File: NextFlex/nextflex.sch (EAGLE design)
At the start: 2 parts, among them J1 FFC-32, J2 FFC-32

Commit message: more nextflex progress
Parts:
- added C1, C2, C7, C8: 1uF, scono:CAP0603-CAP
- added C3, C4: 18pF, scono:CAP0603-CAP
- added C5, C6: 2.2uF, scono:CAP0603-CAP
- added D1, D2: (no value), scono:DIODE_CZRU
- added D4, D7: RED, scono:LED0603
- added D5: NIR, scono:LED0603
- added D6: OPD, scono:LED1206
- added D8: YELLOW, scono:LED0603
- added D9: GREEN, scono:LED0603
- added J3: (no value), scono:CONN_10"
- added J4, J5: (no value), scono:CONN_02
- added J6: (no value), scono:CONN_06SILK_FEMALE_PTH
- added J7: (no value), scono:CONN_04
- added J8: FFC-32, scono:FFC-32
- added JP1, JP2: JUMPER-SMT_2_NC_TRACE_NO-SILK, scono:JUMPER-SMT_2_NC_TRACE_NO-SILK
- added Q1: (no value), scono:CRYSTAL_ECS_8MHZ
- added R1, R2: 10k, scono:R-US_0603
- added R3: 330R, scono:RES_BUS
- added R7, R8: 330R, scono:R-US_0603
- added R9: 1k, scono:R-US_0603
- added R_CAL, R_FB: 100k, scono:R-US_0603
- added S1: (no value), scono:DP3T
- added TP3, TP4, VIN, VOUT: TEST_POINTTHRU, scono:TEST_POINTTHRU
- added U1, U2: DG406DYZ-T, scono:DG406DYZ-T
- added U3: AD5933YRSZ, scono:AD5933YRSZ
- added U4: AFE4490_AFE4490, scono:AFE4490_AFE4490
- added U5: AZ1117EH-3.3TRG1, scono:AZ1117EH-3.3TRG1
- added U6: LM340SX-5.0/NOPB, scono:LM340SX-5.0/NOPB
- J2: value FFC-32 -> (none); device scono:FFC-32 -> scono:CONN_02
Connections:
- new net 3.3V: C2.1, C7.1, D7.A, JP2.2, U4.!AFE_PDN, U4.!RESET, U4.RX_ANA_SUP@1, U4.RX_ANA_SUP@2, U4.RX_DIG_SUP, U5.OUT
- new net 5V: C8.1, J6.6, U4.LED_DRV_SUP@1, U4.LED_DRV_SUP@2, U4.TX_CTRL_SUP, U5.IN
- new net 9V: J8.11, J8.12, J8.27, J8.28
- new net ADC_RDY: U4.ADC_RDY
- new net BG: C5.1, U4.BG
- new net E1: J1.1, J1.2, U1.S1, U2.S1
- new net E10: J1.19, J1.20, U1.S10, U2.S10
- new net E11: J1.21, J1.22, U1.S11, U2.S11
- new net E12: J1.23, J1.24, U1.S12, U2.S12
- new net E13: J1.25, J1.26, U1.S13, U2.S13
- new net E14: J1.27, J1.28, U1.S14, U2.S14
- new net E15: J1.29, J1.30, U1.S15, U2.S15
- new net E2: J1.3, J1.4, U1.S2, U2.S2
- new net E3: J1.5, J1.6, U1.S3, U2.S3
- new net E4: J1.7, J1.8, U1.S4, U2.S4
- new net E5: J1.10, J1.9, U1.S5, U2.S5
- new net E6: J1.11, J1.12, U1.S6, U2.S6
- new net E7: J1.13, J1.14, U1.S7, U2.S7
- new net E8: J1.15, J1.16, U1.S8, U2.S8
- new net E9: J1.17, J1.18, U1.S9, U2.S9
- new net GND: C1.1, C2.2, C3.2, C4.2, C5.2, C6.2, C7.2, C8.2, D1.P, D2.P, J5.1, J5.2, J6.1, R3.10, R3.11, R3.12, R3.13, R3.14, R3.15, R3.16, R3.9, U1.GND, U1.V-, U2.GND, U2.V-, U3.AGND1, U3.AGND2, U3.DGND, U4.LED_DRV_GND@1, U4.LED_DRV_GND@2, U4.LED_DRV_GND@3, U4.RX_ANA_GND@1, U4.RX_ANA_GND@2, U4.RX_ANA_GND@3, U4.RX_DIG_GND@1, U4.RX_DIG_GND@2, U4.VSS, U5.ADJ/GND
- new net GRN: D9.A
- new net INN: J7.4, J8.19, J8.20, JP1.2, U4.INN
- new net INP: D6.C, J7.3, J8.23, J8.24, U4.INP
- new net MUX_1_16: R_CAL.1, TP4.P$1, U1.S16
- new net MUX_1_SEL_0: J3.3, U1.A0
- new net MUX_1_SEL_1: J3.4, U1.A1
- new net MUX_1_SEL_2: J3.5, U1.A2
- new net MUX_1_SEL_3: J3.6, U1.A3
- new net MUX_2_16: R_CAL.2, TP3.P$1, U2.S16
- new net MUX_2_SEL_0: J3.7, U2.A0
- new net MUX_2_SEL_1: J3.8, U2.A1
- new net MUX_2_SEL_2: J3.9, U2.A2
- new net MUX_2_SEL_3: J3.10, U2.A3
- new net N$16: D4.A, D5.A, JP2.1
- new net N$17: D5.C, R7.1
- new net N$18: D4.C, R8.1
- new net N$19: D6.A, R9.1
- new net N$20: JP1.1, R9.2
- new net N$3: R_FB.2, U3.RFB
- new net N$5: D7.C, R3.1, R3.2
- new net N$6: D8.C, R3.4, R3.5
- new net N$7: D9.C, R3.7, R3.8
- new net SCL: J3.2, R2.1, U3.SCL
- new net SDA: J3.1, R1.1, U3.SDA
- new net SPI_MISO: J6.3, U4.SPISOMI
- new net SPI_MOSI: J6.4, U4.SPISIMO
- new net SPI_SCLK: J6.2, U4.SCLK
- new net SPI_SEL: J6.5, U4.SPISTE
- new net TXN: D1.N, J7.1, J8.15, J8.16, R7.2, U4.TXN
- new net TXP: D2.N, J7.2, J8.31, J8.32, R8.2, U4.TXP
- new net TX_REF: C6.1, U4.TX_REF
- new net VCC: C1.2, J4.1, J4.2, R1.2, R2.2, U1.EN, U1.V+, U2.EN, U2.V+, U3.AVDD1, U3.AVDD2, U3.DVDD
- new net VIN: J2.1, U2.D, VIN.P$1
- new net VIN_AD: J2.2, R_FB.1, U3.VIN
- new net VOUT: U1.D, U3.VOUT, VOUT.P$1
- new net XIN: C3.1, Q1.A, U4.XIN
- new net XOUT: C4.1, Q1.B, U4.XOUT
- new net YEL: D8.A
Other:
- note added: "AFE4490 SPI"

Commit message: finish rev a of nextflex
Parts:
- removed D7: RED, scono:LED0603
- removed D8: YELLOW, scono:LED0603
- removed D9: GREEN, scono:LED0603
- removed J8: FFC-32, scono:FFC-32
- removed R3: 330R, scono:RES_BUS
- removed S1: (no value), scono:DP3T
- added S2: DPDT-SWITCH, scono:DPDT-SWITCH
- J4: value (none) -> BAT
- J5: value (none) -> FFC-32; device scono:CONN_02 -> scono:FFC-32
- J6: device scono:CONN_06SILK_FEMALE_PTH -> scono:CONN_04
- Q1: device scono:CRYSTAL_ECS_8MHZ -> scono:CRYSTAL_SMOL
- U6: value LM340SX-5.0/NOPB -> LM340MPX-5.0230; device scono:LM340SX-5.0/NOPB -> scono:LM340MPX-5.0230
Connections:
- removed net 9V: J8.11, J8.12, J8.27, J8.28
- removed net GRN: D9.A
- removed net N$5: D7.C, R3.1, R3.2
- removed net N$6: D8.C, R3.4, R3.5
- removed net N$7: D9.C, R3.7, R3.8
- removed net YEL: D8.A
- new net BAT+: J4.2, S2.1
- new net BAT-: J4.1, S2.4
- net 3.3V: no longer D7.A
- net 5V: now also C1.2, R1.2, R2.2, U1.EN, U1.V+, U2.EN, U2.V+, U3.AVDD1, U3.AVDD2, U3.DVDD, U6.5V; no longer J6.6
- net E1: now also J1.31, J1.32; no longer J1.1, J1.2
- net E10: now also J1.13, J1.14; no longer J1.19, J1.20
- net E11: now also J1.11, J1.12; no longer J1.21, J1.22
- net E12: now also J1.10, J1.9; no longer J1.23, J1.24
- net E13: now also J1.7, J1.8; no longer J1.25, J1.26
- net E14: now also J1.5, J1.6; no longer J1.27, J1.28
- net E15: now also J1.3, J1.4; no longer J1.29, J1.30
- net E2: now also J1.29, J1.30; no longer J1.3, J1.4
- net E3: now also J1.27, J1.28; no longer J1.5, J1.6
- net E4: now also J1.25, J1.26; no longer J1.7, J1.8
- net E5: now also J1.23, J1.24; no longer J1.10, J1.9
- net E6: now also J1.21, J1.22; no longer J1.11, J1.12
- net E7: now also J1.19, J1.20; no longer J1.13, J1.14
- net E8: now also J1.17, J1.18; no longer J1.15, J1.16
- net E9: now also J1.15, J1.16; no longer J1.17, J1.18
- net GND: now also S2.5, U6.GND; no longer J5.1, J5.2, J6.1, R3.10, R3.11, R3.12, R3.13, R3.14, R3.15, R3.16, R3.9
- net INN: now also J5.10, J5.9, J7.3; no longer J7.4, J8.19, J8.20
- net INP: now also J5.13, J5.14, J7.2; no longer J7.3, J8.23, J8.24
- net SPI_MOSI: now also J6.2; no longer J6.4
- net SPI_SCLK: now also J6.4; no longer J6.2
- net SPI_SEL: now also J6.1; no longer J6.5
- net TXN: now also J5.5, J5.6, J7.4; no longer J7.1, J8.15, J8.16
- net TXP: now also J5.21, J5.22, J7.1; no longer J7.2, J8.31, J8.32
- net VCC: now also J5.1, J5.17, J5.18, J5.2, S2.2, U6.VIN; no longer C1.2, J4.1, J4.2, R1.2, R2.2, U1.EN, U1.V+, U2.EN, U2.V+, U3.AVDD1, U3.AVDD2, U3.DVDD

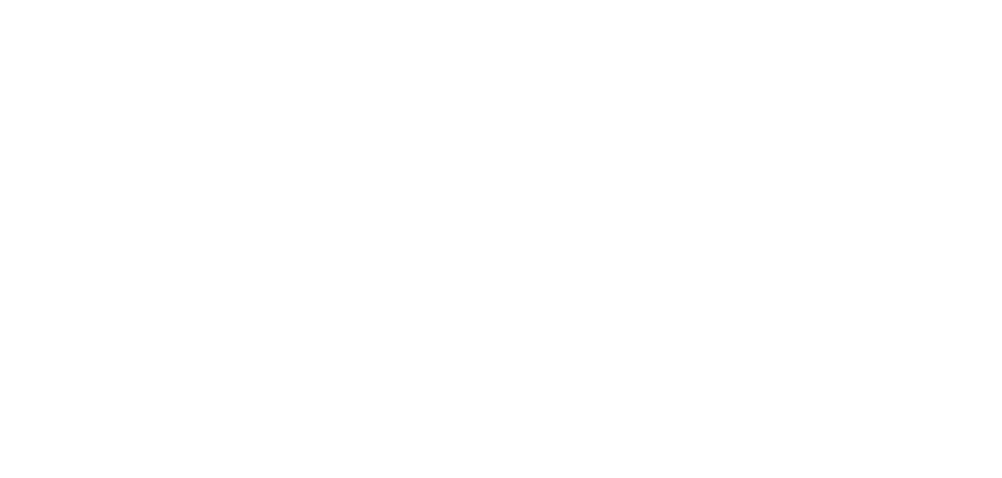
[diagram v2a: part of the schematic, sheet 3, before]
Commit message: Add bom and clp files for jcl
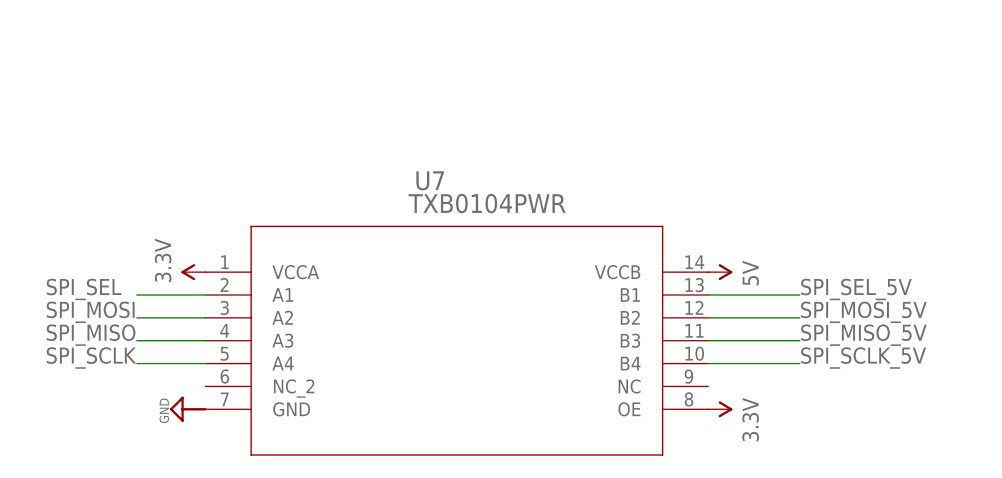
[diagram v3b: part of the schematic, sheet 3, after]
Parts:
- added U7: TXB0104PWR, scono:TXB0104PWR
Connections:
- new net SPI_MISO_5V: J6.3, U7.B3
- new net SPI_MOSI_5V: J6.2, U7.B2
- new net SPI_SCLK_5V: J6.4, U7.B4
- new net SPI_SEL_5V: J6.1, U7.B1
- net 3.3V: now also U7.OE, U7.VCCA
- net 5V: now also U7.VCCB
- net GND: now also U7.GND
- net SPI_MISO: now also U7.A3; no longer J6.3
- net SPI_MOSI: now also U7.A2; no longer J6.2
- net SPI_SCLK: now also U7.A4; no longer J6.4
- net SPI_SEL: now also U7.A1; no longer J6.1
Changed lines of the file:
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@@
 <part name="J5" library="scono" library_urn="urn:adsk.eagle:library:14850048" deviceset="FFC-32" device="" package3d_urn="urn:adsk.eagle:package:14850860/1"/>
 <part name="J6" library="scono" library_urn="urn:adsk.eagle:library:14850048" deviceset="CONN_04" device="" package3d_urn="urn:adsk.eagle:package:38085/1"/>
+<part name="U7" library="scono" library_urn="urn:adsk.eagle:library:14850048" deviceset="TXB0104PWR" device="" package3d_urn="urn:adsk.eagle:package:14850851/1"/>
+<part name="U$2" library="scono" library_urn="urn:adsk.eagle:library:14850048" deviceset="5V" device=""/>
+<part name="U$13" library="scono" library_urn="urn:adsk.eagle:library:14850048" deviceset="3.3V" device=""/>
+<part name="SUPPLY6" library="scono" library_urn="urn:adsk.eagle:library:14850048" deviceset="GND" device=""/>
+<part name="U$14" library="scono" library_urn="urn:adsk.eagle:library:14850048" deviceset="3.3V" device=""/>
 </parts>
 <sheets>
@@
 <pinref part="U4" gate="G$1" pin="SCLK"/>
 </segment>
-<segment>
-<pinref part="J6" gate="G$1" pin="4"/>
-<wire x1="175.26" y1="83.82" x2="177.8" y2="83.82" width="0.1524" layer="91"/>
-<label x="177.8" y="83.82" size="1.778" layer="95"/>
-</segment>
 </net>
 <net name="SPI_MOSI" class="0">
@@
 <pinref part="U4" gate="G$1" pin="SPISIMO"/>
 </segment>
-<segment>
-<pinref part="J6" gate="G$1" pin="2"/>
-<wire x1="175.26" y1="78.74" x2="177.8" y2="78.74" width="0.1524" layer="91"/>
-<label x="177.8" y="78.74" size="1.778" layer="95"/>
-</segment>
 </net>
 <net name="SPI_SEL" class="0">
@@
 <pinref part="U4" gate="G$1" pin="SPISTE"/>
 </segment>
-<segment>
-<pinref part="J6" gate="G$1" pin="1"/>
-<wire x1="175.26" y1="76.2" x2="177.8" y2="76.2" width="0.1524" layer="91"/>
-<label x="177.8" y="76.2" size="1.778" layer="95"/>
-</segment>
 </net>
 <net name="SPI_MISO" class="0">
@@
 <label x="93.98" y="137.16" size="1.778" layer="95"/>
 <pinref part="U4" gate="G$1" pin="SPISOMI"/>
-</segment>
-<segment>
-<pinref part="J6" gate="G$1" pin="3"/>
-<wire x1="175.26" y1="81.28" x2="177.8" y2="81.28" width="0.1524" layer="91"/>
-<label x="177.8" y="81.28" size="1.778" layer="95"/>
 </segment>
 </net>
@@
 <pinref part="J5" gate="G$1" pin="18"/>
 <wire x1="116.84" y1="55.88" x2="116.84" y2="53.34" width="0.1524" layer="91"/>
+</segment>
+</net>
+<net name="SPI_SCLK_5V" class="0">
+<segment>
+<pinref part="J6" gate="G$1" pin="4"/>
+<wire x1="175.26" y1="83.82" x2="177.8" y2="83.82" width="0.1524" layer="91"/>
+<label x="177.8" y="83.82" size="1.778" layer="95"/>
+</segment>
+</net>
+<net name="SPI_MISO_5V" class="0">
+<segment>
+<pinref part="J6" gate="G$1" pin="3"/>
+<wire x1="175.26" y1="81.28" x2="177.8" y2="81.28" width="0.1524" layer="91"/>
+<label x="177.8" y="81.28" size="1.778" layer="95"/>
+</segment>
+</net>
+<net name="SPI_MOSI_5V" class="0">
+<segment>
+<pinref part="J6" gate="G$1" pin="2"/>
+<wire x1="175.26" y1="78.74" x2="177.8" y2="78.74" width="0.1524" layer="91"/>
+<label x="177.8" y="78.74" size="1.778" layer="95"/>
+</segment>
+</net>
+<net name="SPI_SEL_5V" class="0">
+<segment>
+<pinref part="J6" gate="G$1" pin="1"/>
+<wire x1="175.26" y1="76.2" x2="177.8" y2="76.2" width="0.1524" layer="91"/>
+<label x="177.8" y="76.2" size="1.778" layer="95"/>
 </segment>
 </net>
@@
 <attribute name="NAME" x="48.26" y="114.808" size="1.778" layer="95" font="vector"/>
 </instance>
+<instance part="U7" gate="A" x="50.8" y="63.5" smashed="yes">
+<attribute name="NAME" x="76.5556" y="72.6186" size="2.0828" layer="95" ratio="6" rot="SR0"/>
+<attribute name="VALUE" x="75.9206" y="70.0786" size="2.0828" layer="96" ratio="6" rot="SR0"/>
+</instance>
+<instance part="U$2" gate="G$1" x="109.22" y="63.5" smashed="yes" rot="R270">
+<attribute name="VALUE" x="113.03" y="64.77" size="1.778" layer="96" rot="R270"/>
+</instance>
+<instance part="U$13" gate="G$1" x="53.34" y="63.5" smashed="yes" rot="R90">
+<attribute name="VALUE" x="49.53" y="62.23" size="1.778" layer="96" rot="R90"/>
+</instance>
+<instance part="SUPPLY6" gate="GND" x="50.8" y="48.26" smashed="yes" rot="R270">
+<attribute name="VALUE" x="48.26" y="49.53" size="1.016" layer="96" rot="R270"/>
+</instance>
+<instance part="U$14" gate="G$1" x="109.22" y="48.26" smashed="yes" rot="R270">
+<attribute name="VALUE" x="113.03" y="49.53" size="1.778" layer="96" rot="R270"/>
+</instance>
 </instances>
 <busses>
@@
 <pinref part="U$12" gate="G$1" pin="5V"/>
 </segment>
+<segment>
+<pinref part="U7" gate="A" pin="VCCB"/>
+<pinref part="U$2" gate="G$1" pin="5V"/>
+</segment>
 </net>
 <net name="GND" class="0">
@@
 <pinref part="S2" gate="G$1" pin="5"/>
 <pinref part="SUPPLY4" gate="GND" pin="GND"/>
+</segment>
+<segment>
+<pinref part="U7" gate="A" pin="GND"/>
+<pinref part="SUPPLY6" gate="GND" pin="GND"/>
 </segment>
 </net>
@@
 </segment>
 </net>
+<net name="3.3V" class="1">
+<segment>
+<pinref part="U7" gate="A" pin="VCCA"/>
+<pinref part="U$13" gate="G$1" pin="3.3V"/>
+</segment>
+<segment>
+<pinref part="U7" gate="A" pin="OE"/>
+<pinref part="U$14" gate="G$1" pin="3.3V"/>
+</segment>
+</net>
+<net name="SPI_SEL" class="0">
+<segment>
+<pinref part="U7" gate="A" pin="A1"/>
+<wire x1="53.34" y1="60.96" x2="45.72" y2="60.96" width="0.1524" layer="91"/>
+<label x="35.56" y="60.96" size="1.778" layer="95"/>
+</segment>
+</net>
+<net name="SPI_MOSI" class="0">
+<segment>
+<pinref part="U7" gate="A" pin="A2"/>
+<wire x1="53.34" y1="58.42" x2="45.72" y2="58.42" width="0.1524" layer="91"/>
+<label x="35.56" y="58.42" size="1.778" layer="95"/>
+</segment>
+</net>
+<net name="SPI_MISO" class="0">
+<segment>
+<pinref part="U7" gate="A" pin="A3"/>
+<wire x1="53.34" y1="55.88" x2="45.72" y2="55.88" width="0.1524" layer="91"/>
+<label x="35.56" y="55.88" size="1.778" layer="95"/>
+</segment>
+</net>
+<net name="SPI_SCLK" class="0">
+<segment>
+<pinref part="U7" gate="A" pin="A4"/>
+<wire x1="53.34" y1="53.34" x2="45.72" y2="53.34" width="0.1524" layer="91"/>
+<label x="35.56" y="53.34" size="1.778" layer="95"/>
+</segment>
+</net>
+<net name="SPI_SEL_5V" class="0">
+<segment>
+<pinref part="U7" gate="A" pin="B1"/>
+<wire x1="109.22" y1="60.96" x2="119.38" y2="60.96" width="0.1524" layer="91"/>
+<label x="119.38" y="60.96" size="1.778" layer="95"/>
+</segment>
+</net>
+<net name="SPI_MOSI_5V" class="0">
+<segment>
+<pinref part="U7" gate="A" pin="B2"/>
+<wire x1="109.22" y1="58.42" x2="119.38" y2="58.42" width="0.1524" layer="91"/>
+<label x="119.38" y="58.42" size="1.778" layer="95"/>
+</segment>
+</net>
+<net name="SPI_MISO_5V" class="0">
+<segment>
+<pinref part="U7" gate="A" pin="B3"/>
+<wire x1="109.22" y1="55.88" x2="119.38" y2="55.88" width="0.1524" layer="91"/>
+<label x="119.38" y="55.88" size="1.778" layer="95"/>
+</segment>
+</net>
+<net name="SPI_SCLK_5V" class="0">
+<segment>
+<pinref part="U7" gate="A" pin="B4"/>
+<wire x1="109.22" y1="53.34" x2="119.38" y2="53.34" width="0.1524" layer="91"/>
+<label x="119.38" y="53.34" size="1.778" layer="95"/>
+</segment>
+</net>

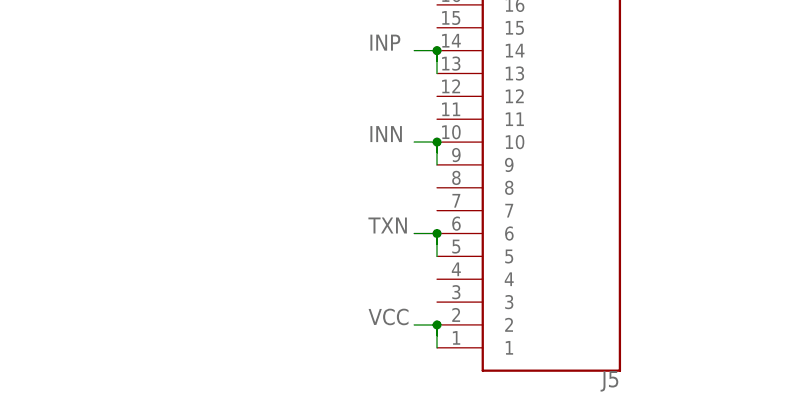
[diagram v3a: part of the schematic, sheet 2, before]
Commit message: small fixes for anode cathone config
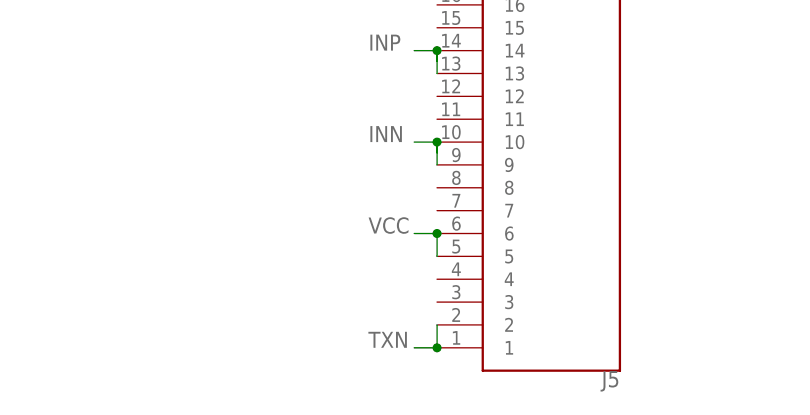
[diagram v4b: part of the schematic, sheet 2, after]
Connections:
- net TXN: now also J5.1, J5.2; no longer J5.5, J5.6
- net VCC: now also J5.5, J5.6; no longer J5.1, J5.2
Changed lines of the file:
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@@
 <?xml version="1.0" encoding="utf-8"?>
 <!DOCTYPE eagle SYSTEM "eagle.dtd">
-<eagle version="9.5.1">
+<eagle version="9.5.2">
 <drawing>
 <settings>
@@
 </segment>
 <segment>
-<wire x1="116.84" y1="25.4" x2="114.3" y2="25.4" width="0.1524" layer="91"/>
-<label x="109.22" y="25.4" size="1.778" layer="95"/>
-<wire x1="116.84" y1="25.4" x2="116.84" y2="24.2062" width="0.1524" layer="91"/>
-<junction x="116.84" y="25.4"/>
-<pinref part="J5" gate="G$1" pin="5"/>
-<pinref part="J5" gate="G$1" pin="6"/>
-<wire x1="116.84" y1="25.4" x2="116.84" y2="22.86" width="0.1524" layer="91"/>
-</segment>
-<segment>
 <pinref part="R7" gate="G$1" pin="2"/>
 <wire x1="50.8" y1="55.88" x2="53.34" y2="55.88" width="0.1524" layer="91"/>
@@
 <wire x1="93.98" y1="63.5" x2="96.52" y2="63.5" width="0.1524" layer="91"/>
 <label x="96.52" y="63.5" size="1.778" layer="95"/>
+</segment>
+<segment>
+<pinref part="J5" gate="G$1" pin="2"/>
+<pinref part="J5" gate="G$1" pin="1"/>
+<wire x1="116.84" y1="15.24" x2="116.84" y2="12.7" width="0.1524" layer="91"/>
+<wire x1="114.3" y1="12.7" x2="116.84" y2="12.7" width="0.1524" layer="91"/>
+<junction x="116.84" y="12.7"/>
+<label x="109.22" y="12.7" size="1.778" layer="95"/>
 </segment>
 </net>
@@
 <net name="VCC" class="1">
 <segment>
-<wire x1="116.84" y1="15.24" x2="114.3" y2="15.24" width="0.1524" layer="91"/>
-<label x="109.22" y="15.24" size="1.778" layer="95"/>
-<wire x1="116.84" y1="15.24" x2="116.84" y2="14.0462" width="0.1524" layer="91"/>
-<junction x="116.84" y="15.24"/>
-<pinref part="J5" gate="G$1" pin="1"/>
-<pinref part="J5" gate="G$1" pin="2"/>
-<wire x1="116.84" y1="12.7" x2="116.84" y2="15.24" width="0.1524" layer="91"/>
-</segment>
-<segment>
 <wire x1="116.84" y1="55.88" x2="114.3" y2="55.88" width="0.1524" layer="91"/>
 <label x="109.22" y="55.88" size="1.778" layer="95"/>
@@
 <wire x1="116.84" y1="55.88" x2="116.84" y2="53.34" width="0.1524" layer="91"/>
 </segment>
-</net>
+<segment>
+<pinref part="J5" gate="G$1" pin="5"/>
+<pinref part="J5" gate="G$1" pin="6"/>
+<wire x1="116.84" y1="22.86" x2="116.84" y2="25.4" width="0.1524" layer="91"/>
+<wire x1="114.3" y1="25.4" x2="116.84" y2="25.4" width="0.1524" layer="91"/>
+<junction x="116.84" y="25.4"/>
+<label x="109.22" y="25.4" size="1.778" layer="95"/>
+</segment>
+</net>
